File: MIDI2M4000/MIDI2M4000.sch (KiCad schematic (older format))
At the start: 40 parts, among them J1 MIDI_THRU, J2 BOOT_JMP, J3 MIDI_IN, J4 DEBUG, J5 USER PORT, J6 5V_POWER, J7 SPARE_PINS, SW1 RESET, SW2 SET_CHAN, U1 74LV14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

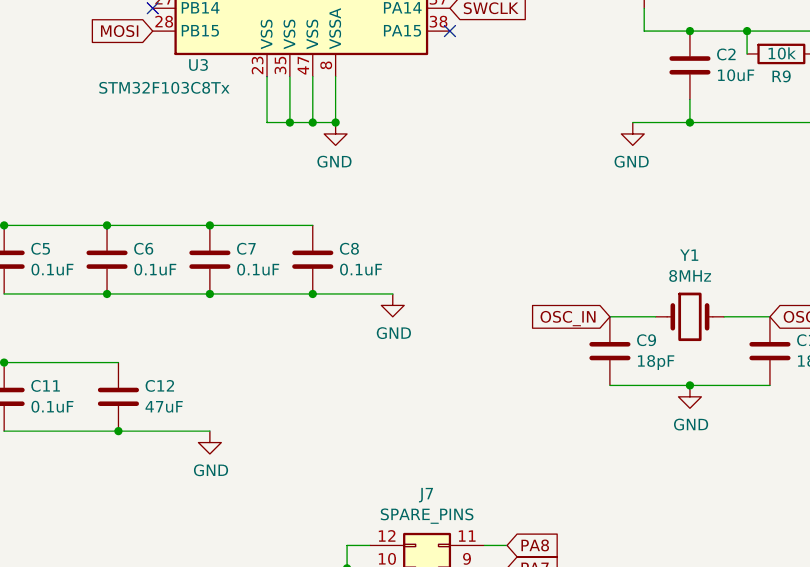
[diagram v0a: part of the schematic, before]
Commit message: Added another decoupler for optoisolator.
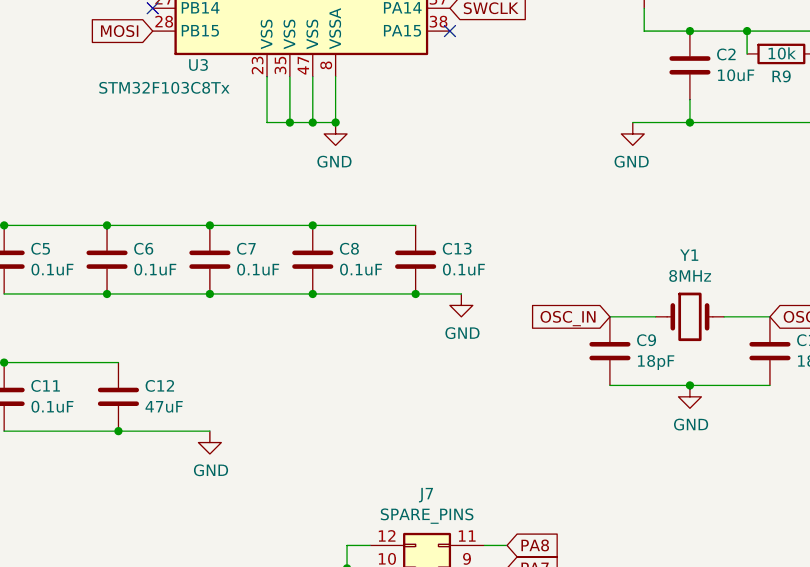
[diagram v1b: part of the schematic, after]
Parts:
- added C13: 0.1uF, Capacitor_SMD:C_0805_2012Metric, symbol Device:C
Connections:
- net +3V3: now also C13.1
- net GND: now also C13.2
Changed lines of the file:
@@
-	1    0    0    -1
-$EndComp
-$Comp
-L power:GND #PWR028
-U 1 1 5CF69FD6
-P 3750 5300
-F 0 "#PWR028" H 3750 5050 50  0001 C CNN
-F 1 "GND" H 3755 5127 50  0000 C CNN
-F 2 "" H 3750 5300 50  0001 C CNN
-F 3 "" H 3750 5300 50  0001 C CNN
-	1    3750 5300
 	1    0    0    -1
 $EndComp
@@
 	2950 5000 3400 5000
 Connection ~ 2950 5000
-Wire Wire Line
-	3750 5300 3400 5300
 Wire Wire Line
 	3400 5300 2950 5300
@@
 Wire Wire Line
 	2550 5900 2950 5900
+$Comp
+L power:GND #PWR028
+U 1 1 5CF69FD6
+P 4050 5300
+F 0 "#PWR028" H 4050 5050 50  0001 C CNN
+F 1 "GND" H 4055 5127 50  0000 C CNN
+F 2 "" H 4050 5300 50  0001 C CNN
+F 3 "" H 4050 5300 50  0001 C CNN
+	1    4050 5300
+	1    0    0    -1
+$EndComp
+$Comp
+L Device:C C13
+U 1 1 5D157C71
+P 3850 5150
+F 0 "C13" H 3965 5196 50  0000 L CNN
+F 1 "0.1uF" H 3965 5105 50  0000 L CNN
+F 2 "Capacitor_SMD:C_0805_2012Metric" H 3888 5000 50  0001 C CNN
+F 3 "~" H 3850 5150 50  0001 C CNN
+	1    3850 5150
+	1    0    0    -1
+$EndComp
+Wire Wire Line
+	3400 5300 3850 5300
+Wire Wire Line
+	3850 5300 4050 5300
+Connection ~ 3850 5300
+Wire Wire Line
+	3400 5000 3850 5000
+Connection ~ 3400 5000
 $EndSCHEMATC

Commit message: Revised LED Resistor Values
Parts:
- J1, J3: symbol Connector:DIN-5-MIDI -> MIDI2M4000-rescue:DIN-5-MIDI-Connector
- R10, R5: value 560R -> 100R
- R4: value 1K -> 220R
- U2: symbol dk_Optoisolators-Logic-Output:TLP2361_TPL_E -> MIDI2M4000-rescue:TLP2361_TPL_E-dk_Optoisolators-Logic-Output
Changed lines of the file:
@@
 $EndDescr
 $Comp
-L dk_Optoisolators-Logic-Output:TLP2361_TPL_E U2
+L MIDI2M4000-rescue:TLP2361_TPL_E-dk_Optoisolators-Logic-Output U2
 U 1 1 5CEACD32
 P 7900 2700
@@
 	9950 2700 9950 1400
 $Comp
-L Connector:DIN-5-MIDI J1
+L MIDI2M4000-rescue:DIN-5-MIDI-Connector J1
 U 1 1 5CEEBE38
 P 7300 1400
@@
 $EndComp
 $Comp
-L Connector:DIN-5-MIDI J3
+L MIDI2M4000-rescue:DIN-5-MIDI-Connector J3
 U 1 1 5CEECEDF
 P 6450 2700
@@
 P 5100 2000
 F 0 "R5" V 5200 2000 50  0000 C CNN
-F 1 "560R" V 5100 2000 50  0000 C CNN
+F 1 "100R" V 5100 2000 50  0000 C CNN
 F 2 "Resistor_SMD:R_0805_2012Metric" V 5030 2000 50  0001 C CNN
 F 3 "~" H 5100 2000 50  0001 C CNN
@@
 P 9250 1550
 F 0 "R4" V 9350 1550 50  0000 C CNN
-F 1 "1K" V 9250 1550 50  0000 C CNN
+F 1 "220R" V 9250 1550 50  0000 C CNN
 F 2 "Resistor_SMD:R_0805_2012Metric" V 9180 1550 50  0001 C CNN
 F 3 "~" H 9250 1550 50  0001 C CNN
@@
 P 8350 5500
 F 0 "R10" V 8450 5500 50  0000 C CNN
-F 1 "560R" V 8350 5500 50  0000 C CNN
+F 1 "100R" V 8350 5500 50  0000 C CNN
 F 2 "Resistor_SMD:R_0805_2012Metric" V 8280 5500 50  0001 C CNN
 F 3 "~" H 8350 5500 50  0001 C CNN
